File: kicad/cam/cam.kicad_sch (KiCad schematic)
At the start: 3 parts, among them U1 S13V10FS, U2 ESP32-CAM

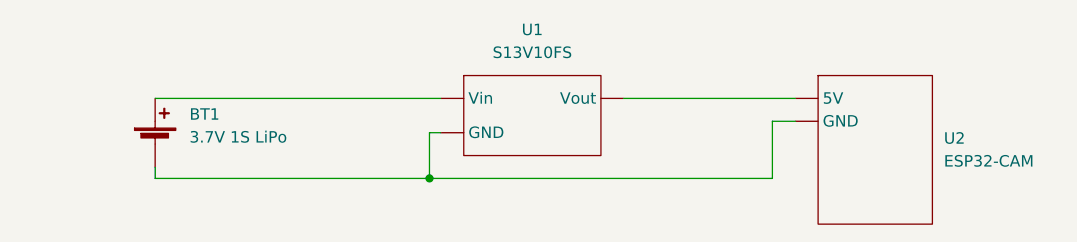
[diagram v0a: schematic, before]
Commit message: Changed library path, main_v1-4 and cam_v1-1 and Project-OWL block diagrams
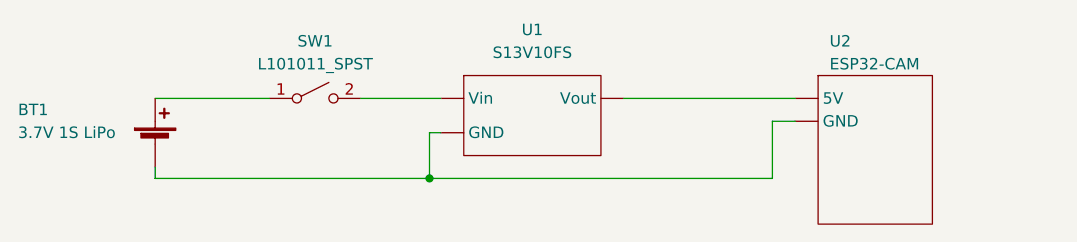
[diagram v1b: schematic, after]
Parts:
- added SW1: L101011_SPST, symbol Switch:SW_SPST
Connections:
- net at U1. (Vout): now also SW1.2 (B); no longer BT1.1 (+)
- new net: BT1.2 (-), U1. (Vout), U2. (GND)
- new net: BT1.1 (+), SW1.1 (A)
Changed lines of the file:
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@@
     (title "Payload Camera Circuit")
     (date "2022-12-16")
-    (rev "1.0")
+    (rev "1.1")
   )
   (junction (at 90.17 66.04) (diameter 0) (color 0 0 0 0)
@@
     (stroke (width 0) (type default) (color 0 0 0 0))
   )
-  (wire (pts (xy 59.69 57.15) (xy 91.44 57.15))
+  (wire (pts (xy 82.55 57.15) (xy 91.44 57.15))
+    (stroke (width 0) (type default) (color 0 0 0 0))
+  )
+  (wire (pts (xy 59.69 57.15) (xy 72.39 57.15))
     (stroke (width 0) (type default) (color 0 0 0 0))
   )
@@
   )
   (symbol (lib_id "Device:Battery_Cell") (at 59.69 62.23 0) (unit 1)
-    (in_bom yes) (on_board yes) (fields_autoplaced)
-    (property "Reference" "BT1" (id 0) (at 63.5 58.9279 0)
+    (in_bom yes) (on_board yes)
+    (property "Reference" "BT1" (id 0) (at 44.45 58.42 0)
       (effects (font (size 1.27 1.27)) (justify left))
     )
-    (property "Value" "3.7V 1S LiPo" (id 1) (at 63.5 61.4679 0)
+    (property "Value" "3.7V 1S LiPo" (id 1) (at 44.45 60.96 0)
       (effects (font (size 1.27 1.27)) (justify left))
     )
@@
   )
   (symbol (lib_id "payload_symbol_library:ESP32-CAM") (at 139.7 52.07 0) (unit 1)
-    (in_bom yes) (on_board yes) (fields_autoplaced)
-    (property "Reference" "U2" (id 0) (at 147.32 61.5949 0)
+    (in_bom yes) (on_board yes)
+    (property "Reference" "U2" (id 0) (at 134.62 50.8 0)
       (effects (font (size 1.27 1.27)) (justify left))
     )
-    (property "Value" "ESP32-CAM" (id 1) (at 147.32 64.1349 0)
+    (property "Value" "ESP32-CAM" (id 1) (at 134.62 53.34 0)
       (effects (font (size 1.27 1.27)) (justify left))
     )
@@
     (pin "")
   )
+  (symbol (lib_id "Switch:SW_SPST") (at 77.47 57.15 0) (unit 1)
+    (in_bom yes) (on_board yes) (fields_autoplaced)
+    (property "Reference" "SW1" (id 0) (at 77.47 50.8 0))
+    (property "Value" "L101011_SPST" (id 1) (at 77.47 53.34 0))
+    (property "Footprint" "" (id 2) (at 77.47 57.15 0)
+      (effects (font (size 1.27 1.27)) hide)
+    )
+    (property "Datasheet" "~" (id 3) (at 77.47 57.15 0)
+      (effects (font (size 1.27 1.27)) hide)
+    )
+    (pin "1")
+    (pin "2")
+  )
   (sheet_instances
     (path "/" (page "1"))
@@
       (reference "BT1") (unit 1) (value "3.7V 1S LiPo") (footprint "")
     )
+    (path "/d1891484-f2a6-457e-924d-ce3e4f9d53ae"
+      (reference "SW1") (unit 1) (value "L101011_SPST") (footprint "")
+    )
     (path "/70068c15-41a7-4281-88d5-2d9751a9bcef"

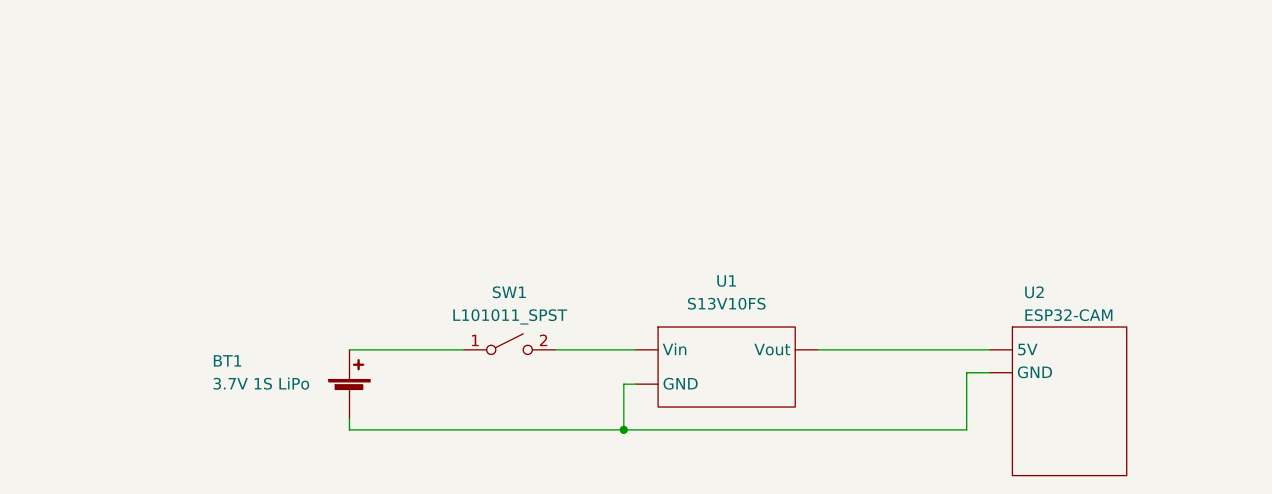
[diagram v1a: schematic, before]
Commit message: Main 1.6, Cam 1.2, added pwr flags and not connected markers to eliminate ERC violations
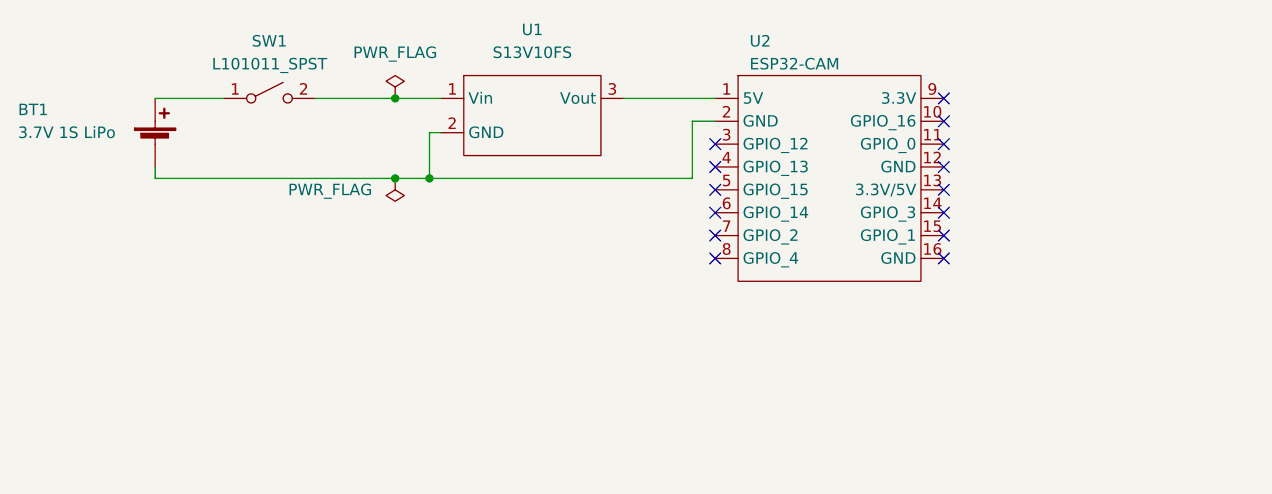
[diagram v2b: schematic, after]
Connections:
- net at SW1.2 (B): now also U1.1 (Vin); no longer U1. (Vout)
- new net: BT1.2 (-), U1.2 (GND), U2.2 (GND)
- new net: U1.3 (Vout), U2.1 (5V)
- no-connect marks 0 -> 14
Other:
- title: Payload Camera Circuit -> Payload Camera Subsystem
- moved on the sheet: BT1, SW1

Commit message: Cape 1.3, Main 1.7
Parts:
- U1: value S13V10FS -> S13V10F5
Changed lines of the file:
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@@
     (in_bom yes) (on_board yes) (fields_autoplaced)
     (property "Reference" "U1" (id 0) (at 80.01 21.59 0))
-    (property "Value" "S13V10FS" (id 1) (at 80.01 24.13 0))
+    (property "Value" "S13V10F5" (id 1) (at 80.01 24.13 0))
     (property "Footprint" "" (id 2) (at 87.63 26.67 0)
       (effects (font (size 1.27 1.27)) hide)
@@
     )
     (path "/70068c15-41a7-4281-88d5-2d9751a9bcef"
-      (reference "U1") (unit 1) (value "S13V10FS") (footprint "")
+      (reference "U1") (unit 1) (value "S13V10F5") (footprint "")
     )
     (path "/8be02d02-d42c-4113-9745-fb4efcc193ff"

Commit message: Updated all schematics
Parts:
- removed SW1: L101011_SPST, symbol Switch:SW_SPST
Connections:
- net at U1.1 (Vin): now also BT1.1 (+)
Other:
- company: (none) -> Peter Costescu
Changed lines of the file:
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@@
     (title "Payload Camera Subsystem")
     (date "2022-12-29")
-    (rev "1.2")
+    (rev "1.3")
+    (company "Peter Costescu")
   )
   (junction (at 68.58 38.1) (diameter 0) (color 0 0 0 0)
@@
     (stroke (width 0) (type default) (color 0 0 0 0))
   )
-  (wire (pts (xy 55.88 29.21) (xy 64.77 29.21))
-    (stroke (width 0) (type default) (color 0 0 0 0))
-  )
-  (wire (pts (xy 38.1 29.21) (xy 45.72 29.21))
+  (wire (pts (xy 38.1 29.21) (xy 64.77 29.21))
     (stroke (width 0) (type default) (color 0 0 0 0))
   )
@@
     (stroke (width 0) (type default) (color 0 0 0 0))
   )
-  (image (at 68.58 63.5)
+  (image (at 86.36 63.5)
     (data
       iVBORw0KGgoAAAANSUhEUgAAAbIAAACKCAYAAADPLc9oAAAABHNCSVQICAgIfAhkiAAAAAlwSFlz
@@
     (pin "9")
   )
-  (symbol (lib_id "Switch:SW_SPST") (at 50.8 29.21 0) (unit 1)
-    (in_bom yes) (on_board yes) (fields_autoplaced)
-    (property "Reference" "SW1" (id 0) (at 50.8 22.86 0))
-    (property "Value" "L101011_SPST" (id 1) (at 50.8 25.4 0))
-    (property "Footprint" "" (id 2) (at 50.8 29.21 0)
-      (effects (font (size 1.27 1.27)) hide)
-    )
-    (property "Datasheet" "~" (id 3) (at 50.8 29.21 0)
-      (effects (font (size 1.27 1.27)) hide)
-    )
-    (pin "1")
-    (pin "2")
-  )
   (sheet_instances
     (path "/" (page "1"))
@@
       (reference "BT1") (unit 1) (value "3.7V 1S LiPo") (footprint "")
     )
-    (path "/d1891484-f2a6-457e-924d-ce3e4f9d53ae"
-      (reference "SW1") (unit 1) (value "L101011_SPST") (footprint "")
-    )
     (path "/70068c15-41a7-4281-88d5-2d9751a9bcef"
